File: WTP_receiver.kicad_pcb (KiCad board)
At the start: 2 copper layers, 54 x 86 mm, 1 part

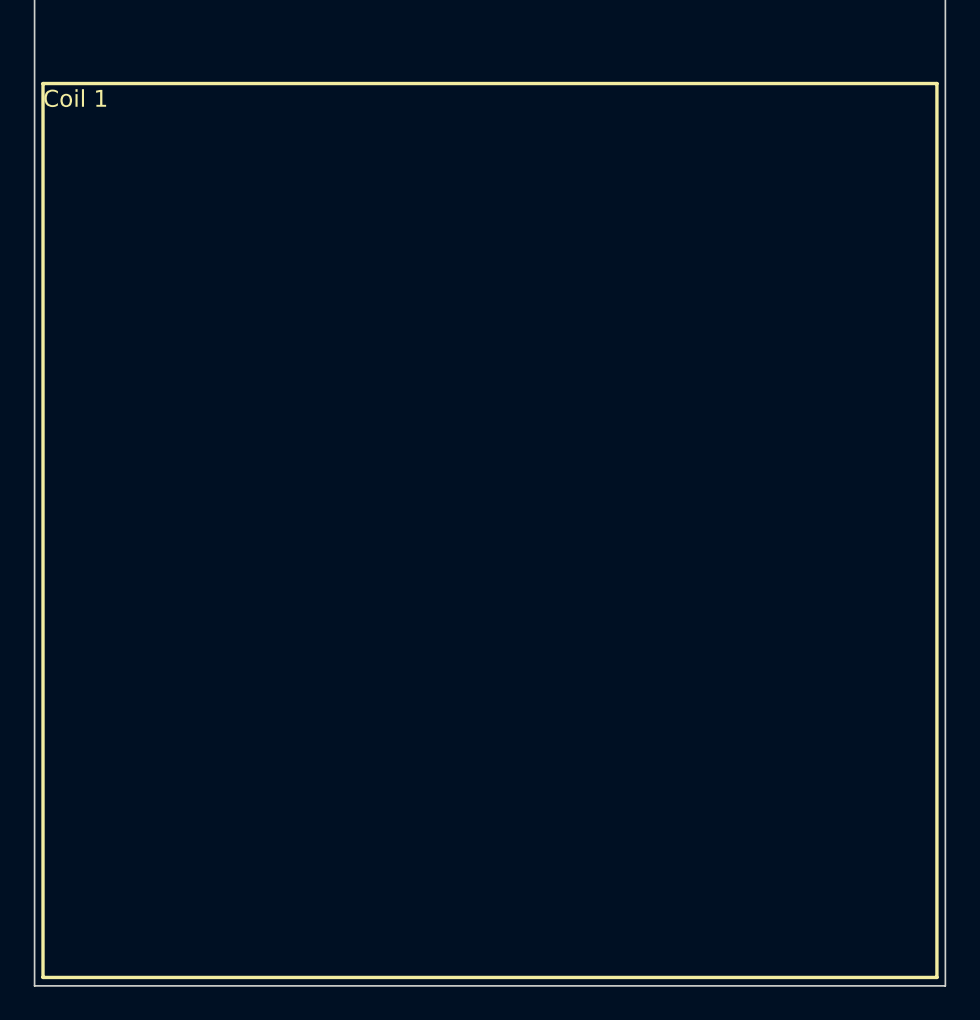
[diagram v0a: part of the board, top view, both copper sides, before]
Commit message: add coil with 44 turns, 0.7mm trace and 10mil spacing for measure
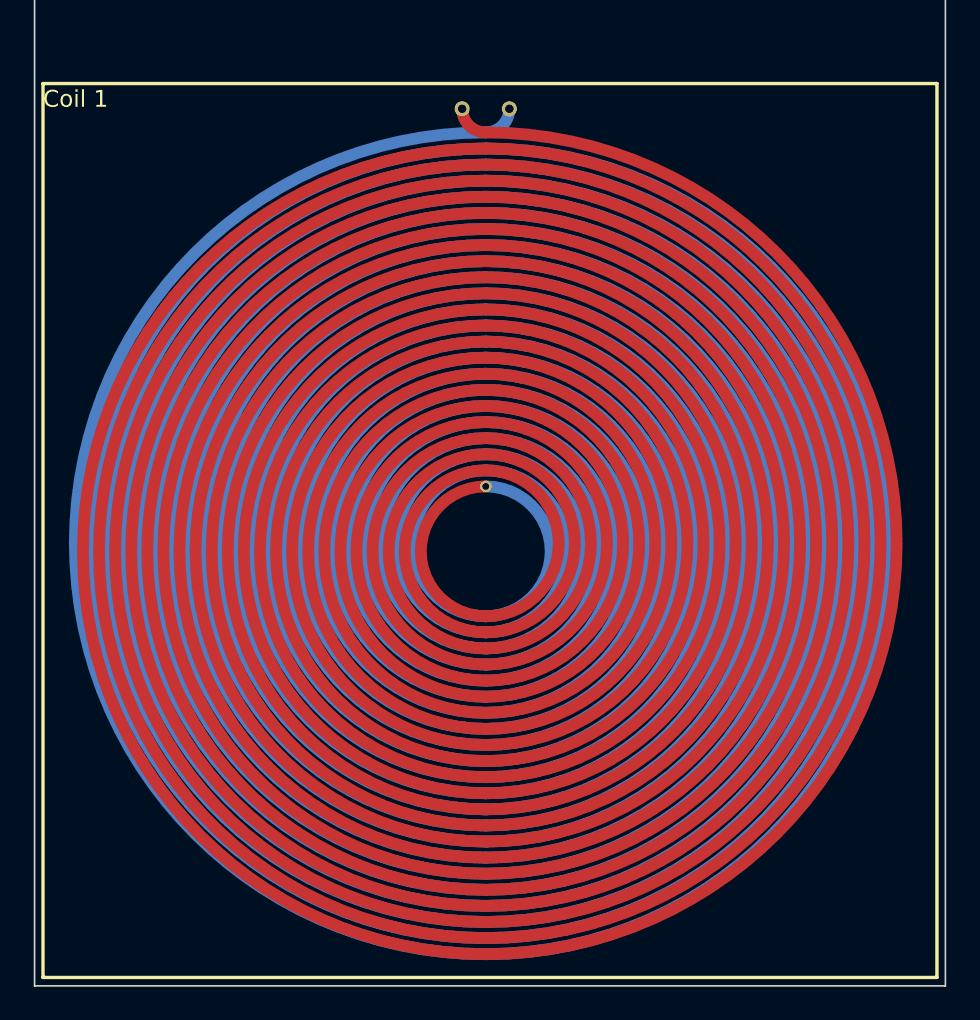
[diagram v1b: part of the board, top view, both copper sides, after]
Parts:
- added REF**: Coil based on ID, Coil based on ID, F.Cu at (142.8, 111.2)

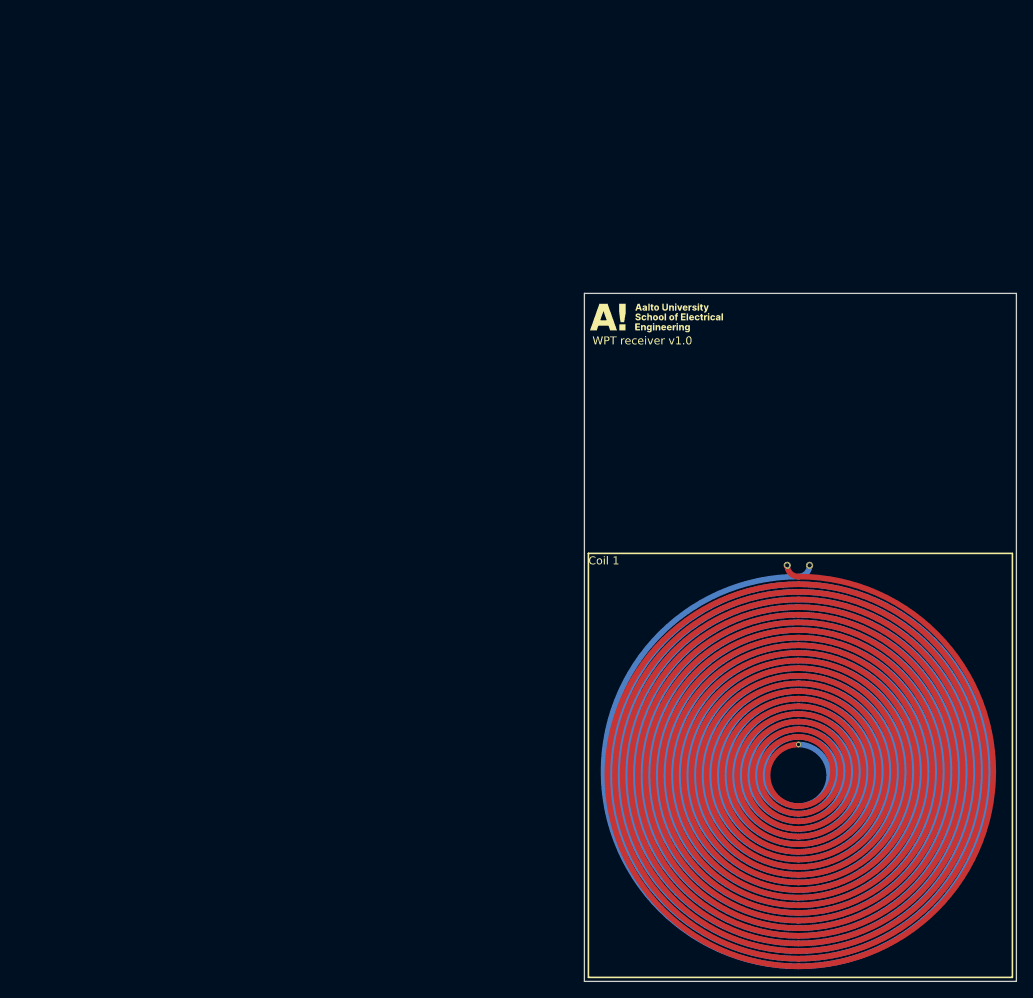
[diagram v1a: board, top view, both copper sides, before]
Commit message: add rectifier circuit to schematic and PCB from old files
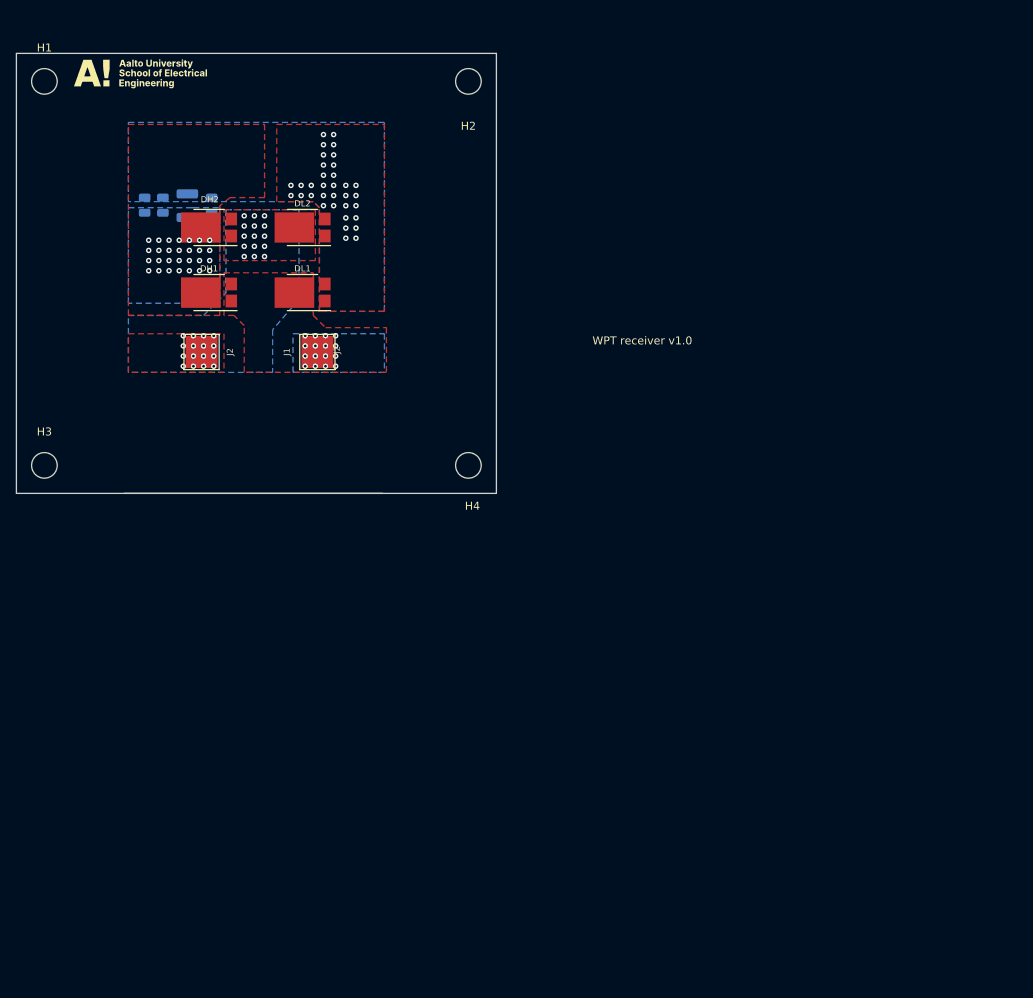
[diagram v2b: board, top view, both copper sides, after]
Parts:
- removed REF**: Coil based on ID, Coil based on ID
- added C1: C, Capacitor_SMD:C_0805_2012Metric, B.Cu at (61.0, 40.0)
- added C2: C, Capacitor_SMD:C_0805_2012Metric, B.Cu at (63.3, 40.0)
- added C3: C, Capacitor_SMD:C_1210_3225Metric, B.Cu at (66.4, 40.0)
- added C4: C, Capacitor_SMD:C_0805_2012Metric, B.Cu at (69.4, 40.0)
- added DH1: PMEG050V030EPD, Package_TO_SOT_SMD:Nexperia_CFP15_SOT-1289, F.Cu at (69.1, 50.9)
- added DH2: PMEG050V030EPD, Package_TO_SOT_SMD:Nexperia_CFP15_SOT-1289, F.Cu at (69.1, 42.8)
- added DL1: PMEG050V030EPD, Package_TO_SOT_SMD:Nexperia_CFP15_SOT-1289, F.Cu at (80.8, 50.9)
- added DL2: PMEG050V030EPD, Package_TO_SOT_SMD:Nexperia_CFP15_SOT-1289, F.Cu at (80.8, 42.8)
- added H1: MountingHole, MountingHole:MountingHole_3.2mm_M3, F.Cu at (48.5, 24.5)
- added H2: MountingHole, MountingHole:MountingHole_3.2mm_M3, F.Cu at (101.5, 24.5)
- added H3: MountingHole, MountingHole:MountingHole_3.2mm_M3, F.Cu at (48.5, 72.5)
- added H4: MountingHole, MountingHole:MountingHole_3.2mm_M3, F.Cu at (101.5, 72.5)
- added J1: Conn_01x01_Male, TestPoint:TestPoint_Pad_4.0x4.0mm, F.Cu at (82.6, 58.3)
- added J2: Conn_01x01_Male, TestPoint:TestPoint_Pad_4.0x4.0mm, F.Cu at (68.1, 58.3)
- moved G*** 71.3 mm to (60.5, 23.5)
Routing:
- net GND: vias 0 -> 34
- net /DC+: vias 0 -> 28
- net /AC2: vias 0 -> 31
- net /AC1: vias 0 -> 16
- added copper zone on B.Cu, net /AC1
- added copper zone on F.Cu, net /AC1
- added copper zone on B.Cu, net /AC2
- added copper zone on F.Cu, net /AC2
- added copper zone on B.Cu, net /DC+
- added copper zone on F.Cu, net /DC+
- added copper zone on B.Cu, net GND
- added copper zone on F.Cu, net GND
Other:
- board size 54 x 86 mm -> 60 x 55 mm
- board text added: "J2"
- board text removed: "Coil 1"
- board text removed: "Coil 2"
- board text removed: "Reserved space for the coils"

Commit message: initial version with traces and components
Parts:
- removed J1, J2: Conn_01x01_Male, TestPoint:TestPoint_Pad_4.0x4.0mm
- added C10: C, Capacitor_SMD:C_1111_2828_metric, F.Cu at (89.0, 70.2)
- added C11: C, Capacitor_SMD:C_1111_2828_metric, F.Cu at (94.0, 70.2)
- added C12: C, Capacitor_SMD:C_1111_2828_metric, F.Cu at (94.0, 58.2)
- added C13: C, Capacitor_SMD:C_1111_2828_metric, F.Cu at (94.0, 62.2)
- added C14: C, Capacitor_SMD:C_1111_2828_metric, F.Cu at (94.0, 66.2)
- added C5: 10uF, Capacitor_SMD:C_1210_3225Metric, B.Cu at (68.0, 35.5)
- added C6: 22uF, Capacitor_SMD:C_0603_1608Metric, B.Cu at (62.4, 34.7)
- added C7: C, Capacitor_SMD:C_1111_2828_metric, F.Cu at (89.0, 58.2)
- added C8: C, Capacitor_SMD:C_1111_2828_metric, F.Cu at (89.0, 62.2)
- added C9: C, Capacitor_SMD:C_1111_2828_metric, F.Cu at (89.0, 66.2)
- added P1: USB_C_Plug_USB2.0, Connector_USB:USB_C_Receptacle_GCT_USB4105-xx-A_16P_TopMnt_Horizontal, F.Cu at (79.8, 25.5)
- added U2: P7815-500R, P7815-500R:CONV_P7815-500R, F.Cu at (65.0, 39.0)
- moved G*** 38.0 mm to (60.7, 61.5)
- moved C1 15.1 mm to (74.0, 32.3)
- moved C2 15.1 mm to (76.3, 32.3)
- moved C3 15.1 mm to (79.4, 32.4)
- moved C4 15.1 mm to (82.4, 32.3)
- moved DH1 15.1 mm to (82.1, 43.3)
- moved DH2 15.1 mm to (82.1, 35.1)
- moved DL1 15.1 mm to (93.8, 43.3)
- moved DL2 15.1 mm to (93.8, 35.1)
- moved H3 6.50 mm to (55.0, 72.5)
- moved H1 6.25 mm to (54.8, 24.5)
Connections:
- net /AC2 renamed /Coil2
- net /DC+ renamed VDC
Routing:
- net +5V: track 0.00 -> 28.2 mm, vias 0 -> 1
- net GND: track 0.00 -> 10.1 mm
- net /AC1: vias 16 -> 0
- added copper zone on F.Cu, net /Coil1
- removed copper zone on B.Cu, net /AC1
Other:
- board size 60 x 55 mm -> 53.5 x 55 mm
- board text added: "Coil"
- board text added: "Tuning capacitors"
- board text removed: "J2"

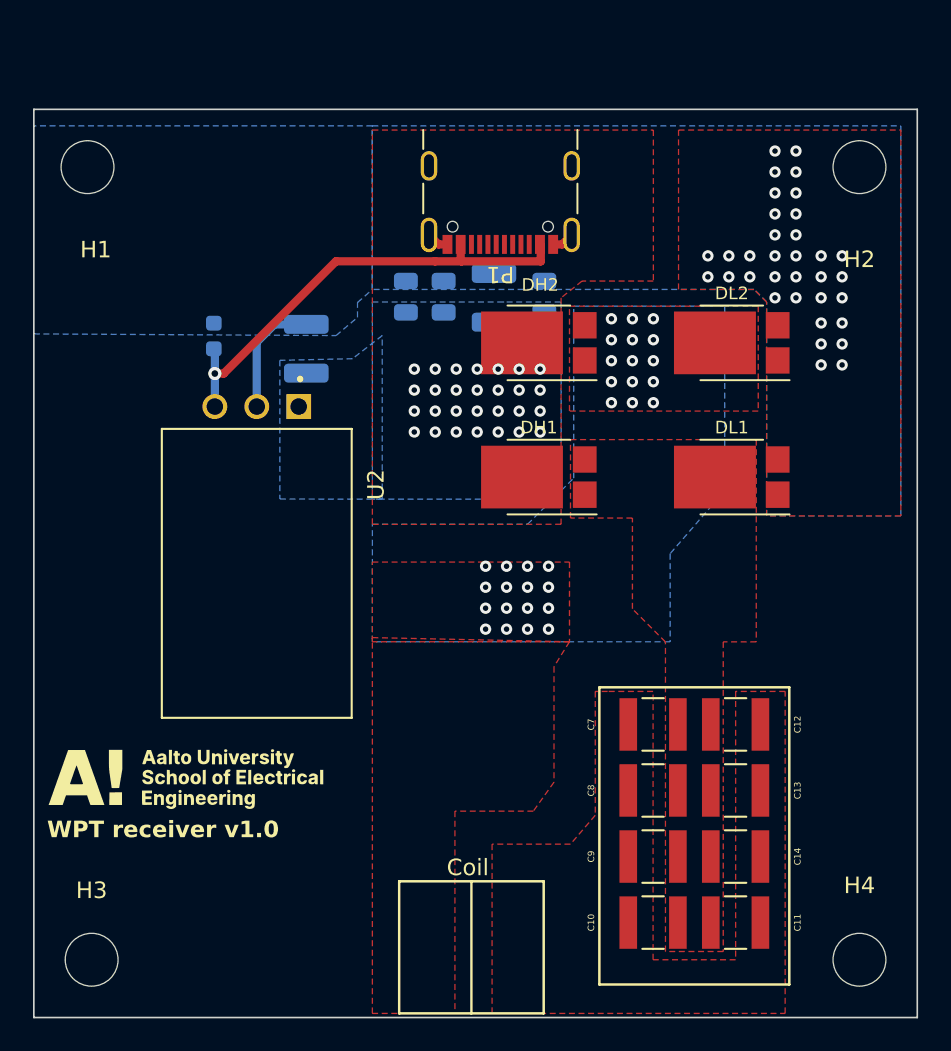
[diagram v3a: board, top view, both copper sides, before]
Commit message: improvements done according to what was agreed in the project meeting
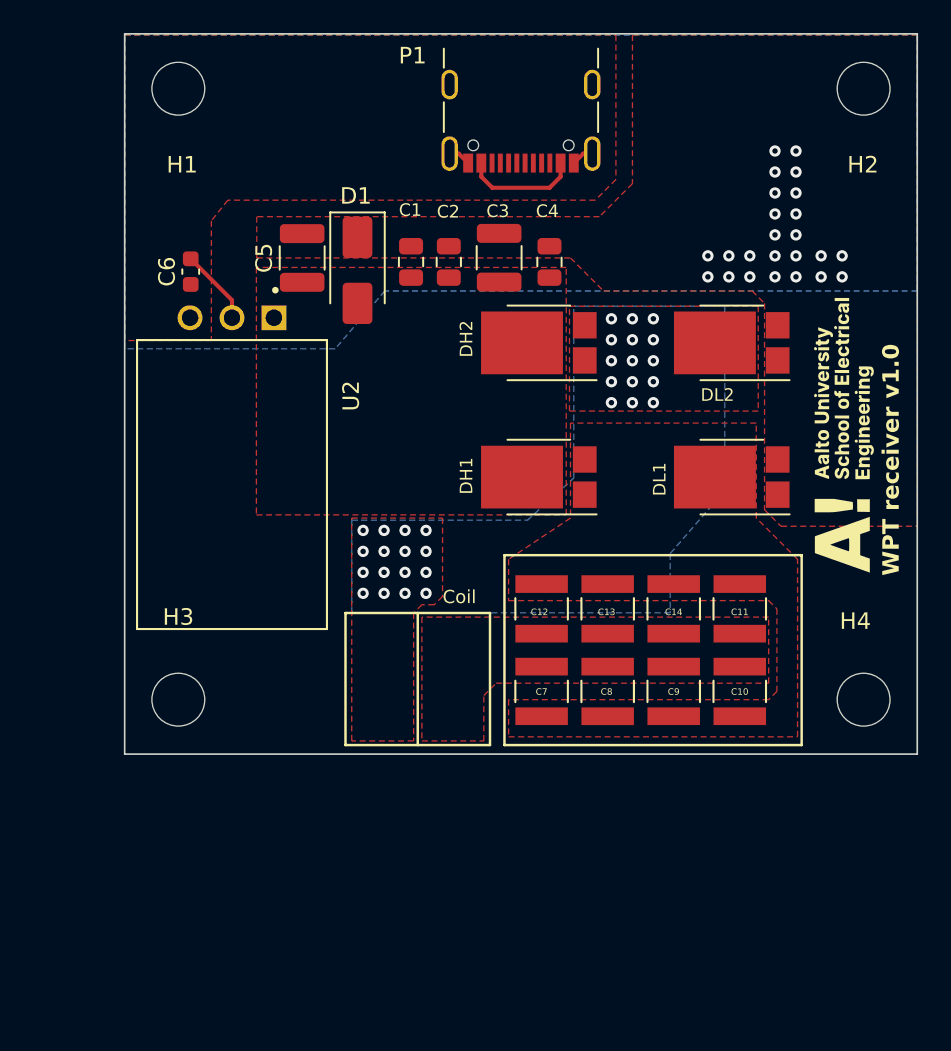
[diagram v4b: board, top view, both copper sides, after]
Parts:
- added D1: D_TVS, Diode_SMD:D_SMA, F.Cu at (71.1, 30.8)
- C1, C2, C3, C4, C5, C6: moved to F.Cu
- moved G*** 44.9 mm to (100.5, 40.8), turned to 90 degrees
- moved C11 19.0 mm to (94.2, 51.3), turned to 90 degrees
- moved H3 16.6 mm to (60.2, 56.8)
- moved H4 15.8 mm to (101.8, 56.8)
- moved C14 15.5 mm to (90.2, 51.3), turned to 90 degrees
- moved C10 15.0 mm to (94.2, 56.2), turned to 90 degrees
- moved C12 13.7 mm to (82.2, 51.3), turned to 90 degrees
- moved C13 13.5 mm to (86.2, 51.3), turned to 90 degrees
- moved C9 10.1 mm to (90.2, 56.2), turned to 90 degrees
- moved H1 7.27 mm to (60.2, 19.8)
- moved C7 7.04 mm to (82.2, 56.2), turned to 90 degrees
- moved C8 6.60 mm to (86.2, 56.3), turned to 90 degrees
- moved U2 5.58 mm to (63.5, 33.6)
- moved C5 5.51 mm to (67.8, 30.0)
- moved P1 5.08 mm to (81.0, 20.6)
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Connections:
- C10 pad 1: /Coil1 -> /AC1
- C10 pad 2: /AC1 -> /Coil1
- C11 pad 1: /AC1 -> /Coil1
- C11 pad 2: /Coil1 -> /AC1
- C12 pad 1: /AC1 -> /Coil1
- C12 pad 2: /Coil1 -> /AC1
- C13 pad 1: /AC1 -> /Coil1
- C13 pad 2: /Coil1 -> /AC1
- C14 pad 1: /AC1 -> /Coil1
- C14 pad 2: /Coil1 -> /AC1
- C7 pad 1: /Coil1 -> /AC1
- C7 pad 2: /AC1 -> /Coil1
- C8 pad 1: /Coil1 -> /AC1
- C8 pad 2: /AC1 -> /Coil1
- C9 pad 1: /Coil1 -> /AC1
- C9 pad 2: /AC1 -> /Coil1
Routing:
- net +5V: track 28.2 -> 7.01 mm, vias 1 -> 0
- net GND: track 10.1 -> 7.32 mm, vias 34 -> 24
- net VDC: vias 28 -> 0
- added copper zone on F.Cu, net +5V
- removed copper zone on B.Cu, net VDC
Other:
- board size 53.5 x 55 mm -> 48 x 43.6 mm

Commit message: generate gerbers, start working with BOM
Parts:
- removed P1: USB_C_Plug_USB2.0, Connector_USB:USB_C_Receptacle_GCT_USB4105-xx-A_16P_TopMnt_Horizontal
- added J3: TYPE-C_16PIN_2MD__073_, components:SHOUHAN_TYPE-C_16PIN_2MD__073_, F.Cu at (81.9, 19.6)
- D1: value D_TVS -> SMAJ85CA-TR
- moved H3 0.55 mm to (60.3, 56.2)
- moved C5 0.55 mm to (67.2, 30.0)
- moved H4 0.45 mm to (101.8, 56.3)
- moved D1 0.20 mm to (71.3, 30.8)
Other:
- board size 48 x 43.6 mm -> 48 x 43.4 mm

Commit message: update BOM and gerbers
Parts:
- C5: footprint Capacitor_SMD:C_1210_3225Metric -> Capacitor_SMD:C_2220_5650Metric
- C6: footprint Capacitor_SMD:C_0603_1608Metric -> Capacitor_SMD:C_0805_2012Metric
- moved H3 1.30 mm to (60.4, 57.5)
- moved U2 1.25 mm to (63.5, 34.9)
- moved H4 1.23 mm to (101.5, 57.5)
- moved C6 1.19 mm to (60.8, 32.0)
- moved D1 0.85 mm to (71.3, 29.9)
- moved C5 0.60 mm to (66.6, 30.0)
- moved C1 0.46 mm to (74.2, 29.8)
- moved C2 0.44 mm to (76.6, 29.8)
- moved C4 0.36 mm to (82.6, 29.9)
- moved H2 0.25 mm to (101.5, 19.8)
- moved H1 0.15 mm to (60.4, 19.8)
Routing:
- net GND: track 7.31 -> 8.02 mm
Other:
- board size 48 x 43.4 mm -> 48 x 44.3 mm
